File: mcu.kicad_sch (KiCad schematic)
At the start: 20 parts, among them Q8 RUM002N05T2L, Q9 RUM002N05T2L, U2 ESP32-WROOM-32D

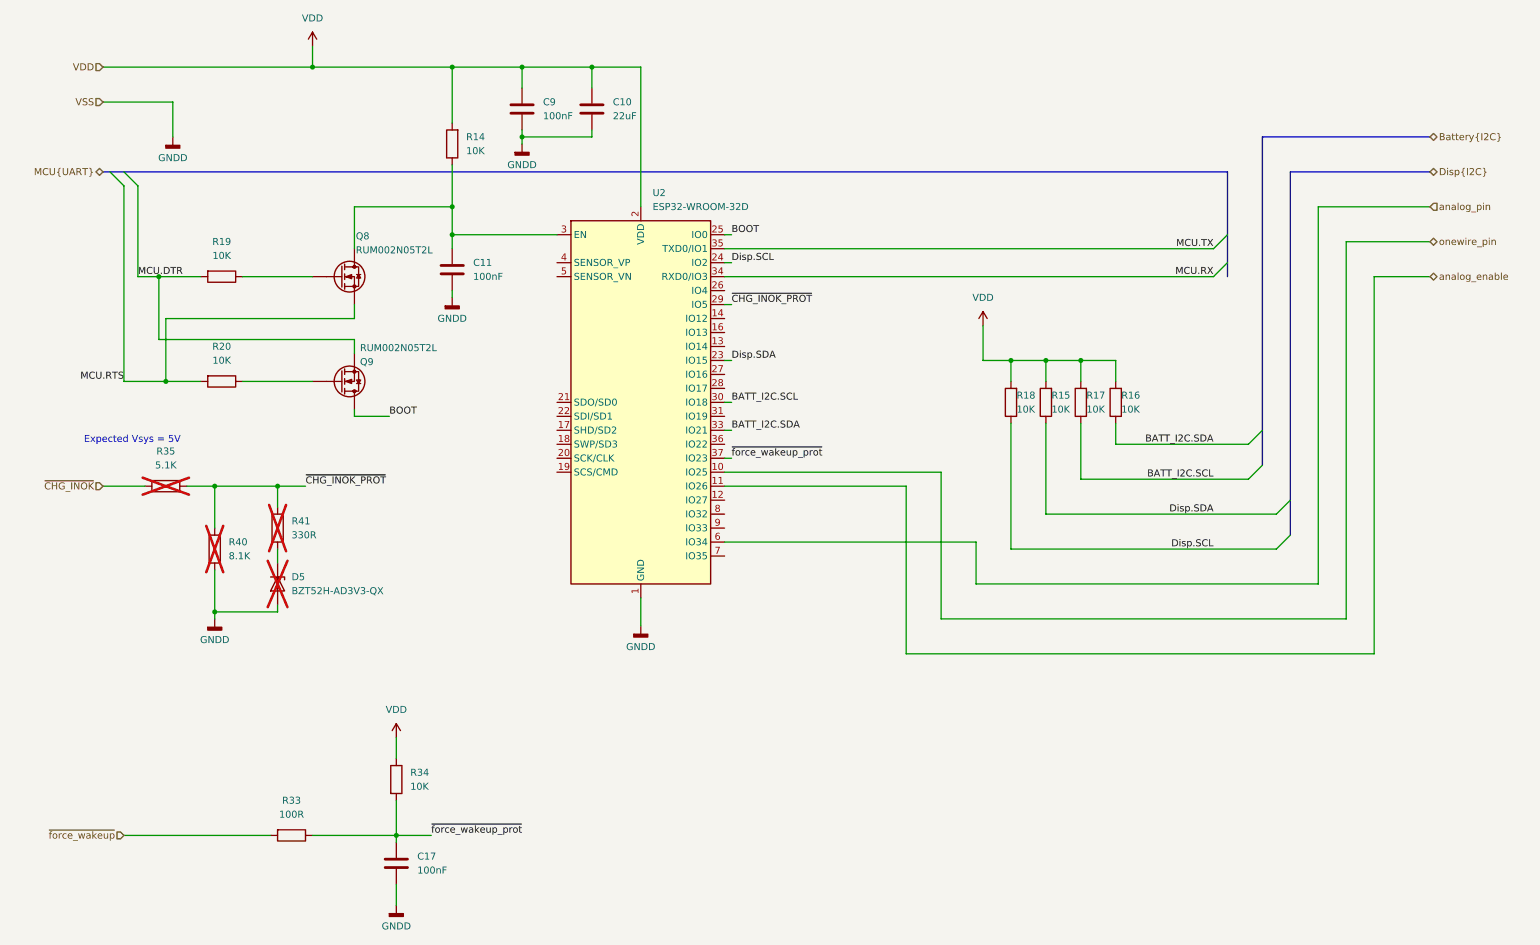
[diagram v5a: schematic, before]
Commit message: Fix issues from Issue#1
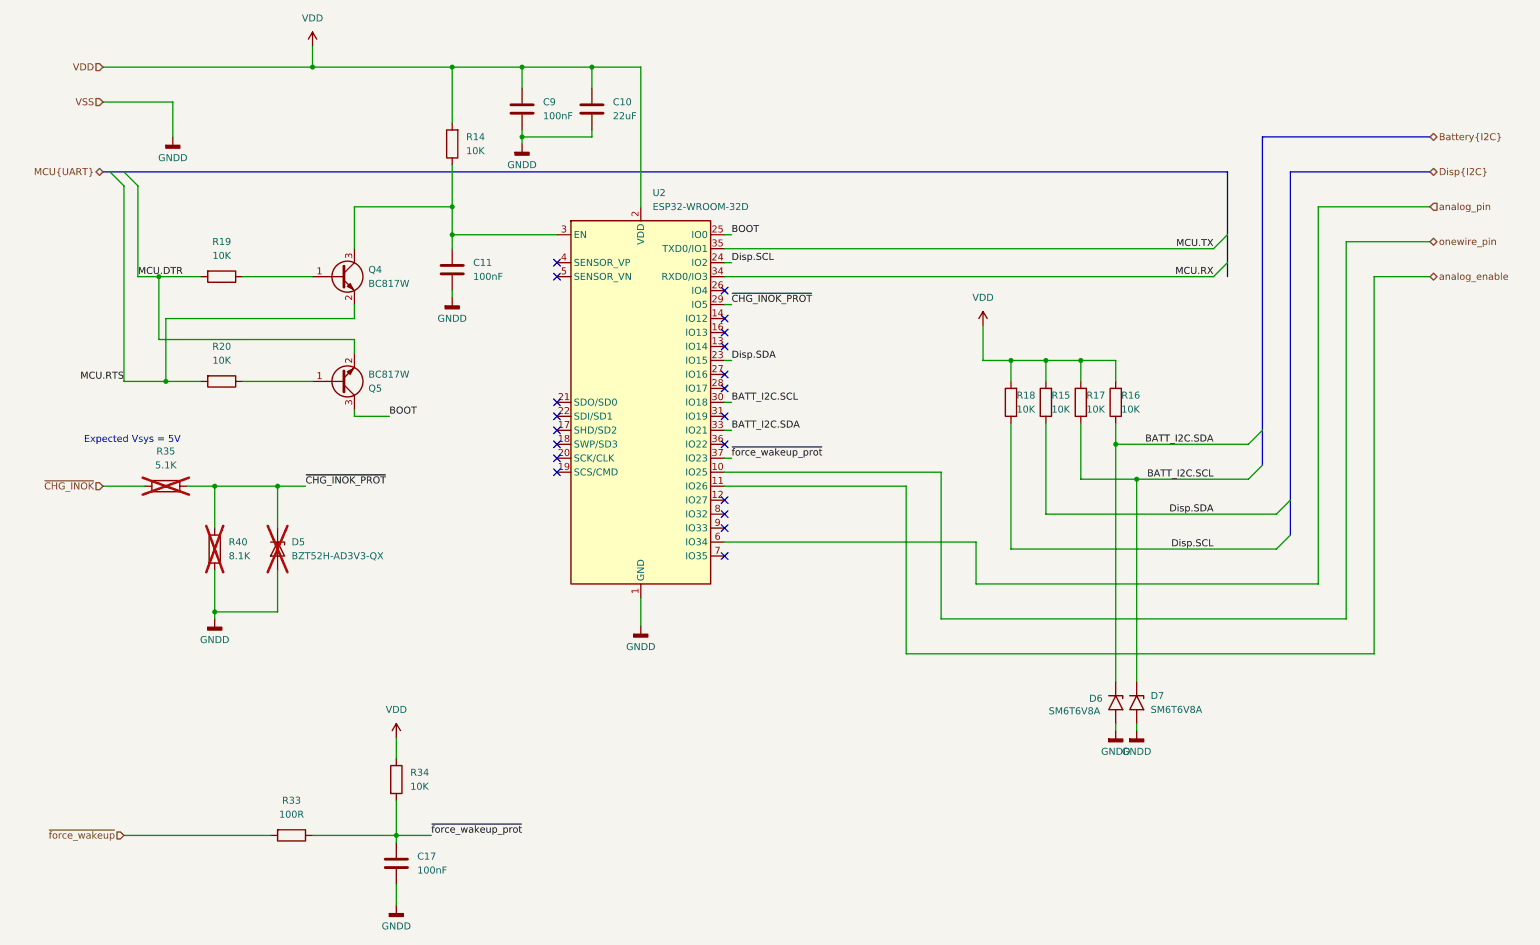
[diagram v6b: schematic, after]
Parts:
- removed Q8, Q9: RUM002N05T2L, Package_TO_SOT_SMD:SOT-723, symbol Device:Q_NMOS
- removed R41: 330R, Resistor_SMD:R_0603_1608Metric_Pad0.98x0.95mm_HandSolder, symbol Device:R
- added D6, D7: SM6T6V8A, Diode_SMD:D_SMB, symbol Diode:SM6T6V8A
- added Q4, Q5: BC817W, Package_TO_SOT_SMD:SOT-323_SC-70, symbol Transistor_BJT:BC817W
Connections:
- net BATT_I2C.SCL: now also D7.1 (A1)
- net BATT_I2C.SDA: now also D6.1 (A1)
- net BOOT: now also Q5.3 (C)
- net GNDD: now also D6.2 (A2), D7.2 (A2)
- net MCU.DTR: now also Q5.2 (E)
- net MCU.RTS: now also Q4.2 (E)
- net ~{CHG_INOK_PROT}: now also D5.1 (K)
- net at R20.1: now also Q5.1 (B)
- net at R19.1: now also Q4.1 (B)
- net at C11.1, R14.1, U2.3 (EN): now also Q4.3 (C)
- no-connect marks 0 -> 20
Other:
- moved on the sheet: D5

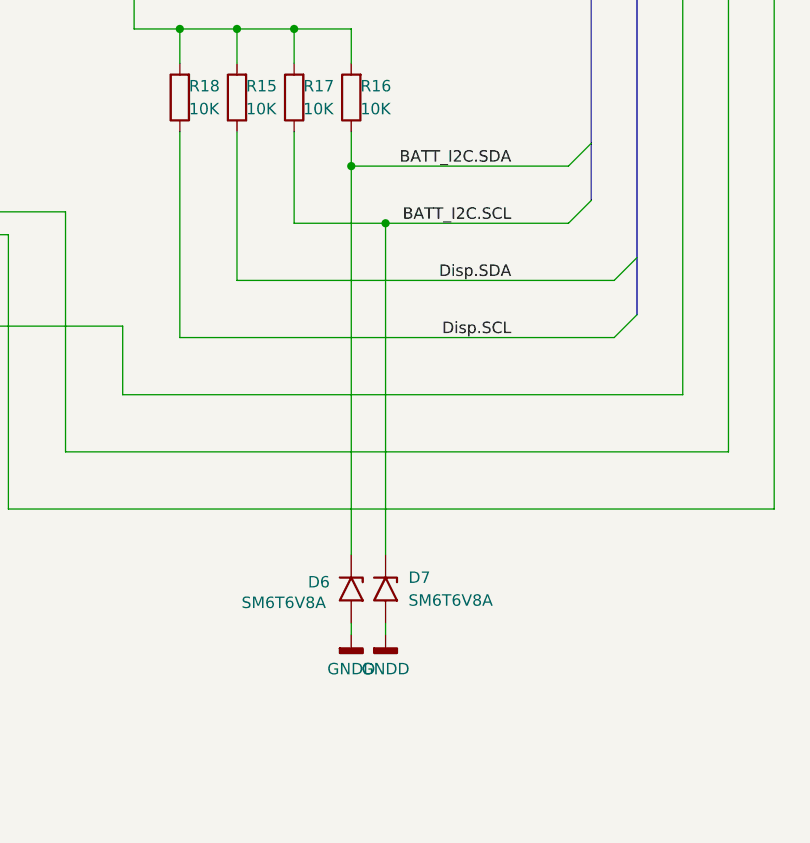
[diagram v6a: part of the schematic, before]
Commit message: Add footprint to debug connector.
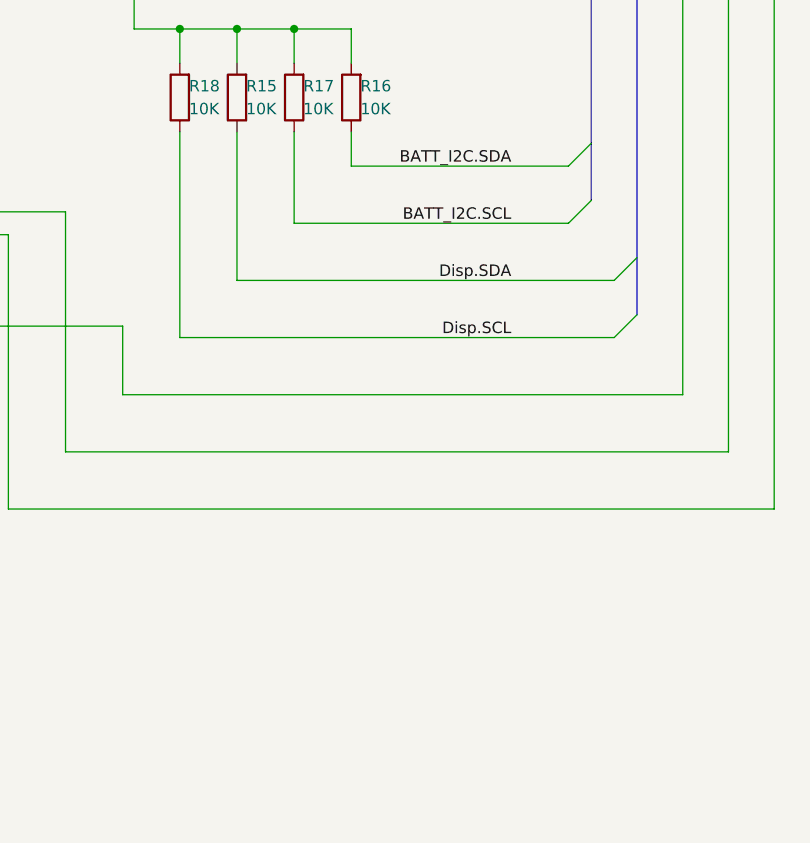
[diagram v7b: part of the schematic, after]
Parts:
- removed D6, D7: SM6T6V8A, Diode_SMD:D_SMB, symbol Diode:SM6T6V8A

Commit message: Add someplacement.
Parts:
- removed U2: ESP32-WROOM-32D, RF_Module:ESP32-WROOM-32D, symbol RF_Module:ESP32-WROOM-32D
- added U2: ESP32-WROOM-32, RF_Module:ESP32-WROOM-32, symbol RF_Module:ESP32-WROOM-32
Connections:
- net BATT_I2C.SCL: now also U2.30 (IO18)
- net BATT_I2C.SDA: now also U2.33 (IO21)
- net BOOT: now also U2.25 (IO0)
- net Disp.SCL: now also U2.24 (IO2)
- net Disp.SDA: now also U2.23 (IO15)
- net GNDD: now also U2.1 (GND), U2.15 (GND), U2.38 (GND), U2.39 (GND)
- net MCU.RX: now also U2.34 (RXD0/IO3)
- net MCU.TX: now also U2.35 (TXD0/IO1)
- net VDD: now also U2.2 (VDD)
- net analog_enable: now also U2.11 (IO26)
- net analog_pin: now also U2.6 (IO34)
- net onewire_pin: now also U2.10 (IO25)
- net ~{CHG_INOK_PROT}: now also U2.29 (IO5)
- net ~{force_wakeup_prot}: now also U2.37 (IO23)
- net at C11.1, Q4.3 (C), R14.1: now also U2.3 (EN)
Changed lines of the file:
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@@
+	)
+	(symbol
+		(lib_id "RF_Module:ESP32-WROOM-32")
+		(at 123.19 86.36 0)
+		(unit 1)
+		(body_style 1)
+		(exclude_from_sim no)
+		(in_bom yes)
+		(on_board yes)
+		(in_pos_files yes)
+		(dnp no)
+		(fields_autoplaced yes)
+		(property "Reference" "U2"
+			(at 125.3333 48.26 0)
+			(show_name no)
+			(do_not_autoplace no)
+			(effects
+				(font
+					(size 1.27 1.27)
+				)
+				(justify left)
+			)
+		)
+		(property "Value" "ESP32-WROOM-32"
+			(at 125.3333 50.8 0)
+			(show_name no)
+			(do_not_autoplace no)
+			(effects
+				(font
+					(size 1.27 1.27)
+				)
+				(justify left)
+			)
+		)
+		(property "Footprint" "RF_Module:ESP32-WROOM-32"
+			(at 123.19 124.46 0)
+			(hide yes)
+			(show_name no)
+			(do_not_autoplace no)
+			(effects
+				(font
+					(size 1.27 1.27)
+				)
+			)
+		)
+		(property "Datasheet" "https://www.espressif.com/sites/default/files/documentation/esp32-wroom-32_datasheet_en.pdf"
+			(at 115.57 85.09 0)
+			(hide yes)
+			(show_name no)
+			(do_not_autoplace no)
+			(effects
+				(font
+					(size 1.27 1.27)
+				)
+			)
+		)
+		(property "Description" "RF Module, ESP32-D0WDQ6 SoC, Wi-Fi 802.11b/g/n, Bluetooth, BLE, 32-bit, 2.7-3.6V, onboard antenna, SMD"
+			(at 123.19 86.36 0)
+			(hide yes)
+			(show_name no)
+			(do_not_autoplace no)
+			(effects
+				(font
+					(size 1.27 1.27)
+				)
+			)
+		)
+		(pin "21"
+		)
+		(pin "12"
+		)
+		(pin "36"
+		)
+		(pin "10"
+		)
+		(pin "26"
+		)
+		(pin "22"
+		)
+		(pin "31"
+		)
+		(pin "23"
+		)
+		(pin "7"
+		)
+		(pin "6"
+		)
+		(pin "5"
+		)
+		(pin "4"
+		)
+		(pin "3"
+		)
+		(pin "2"
+		)
+		(pin "1"
+		)
+		(pin "39"
+		)
+		(pin "35"
+		)
+		(pin "11"
+		)
+		(pin "19"
+		)
+		(pin "17"
+		)
+		(pin "29"
+		)
+		(pin "24"
+		)
+		(pin "8"
+		)
+		(pin "18"
+		)
+		(pin "15"
+		)
+		(pin "32"
+		)
+		(pin "27"
+		)
+		(pin "9"
+		)
+		(pin "38"
+		)
+		(pin "28"
+		)
+		(pin "13"
+		)
+		(pin "20"
+		)
+		(pin "25"
+		)
+		(pin "34"
+		)
+		(pin "30"
+		)
+		(pin "37"
+		)
+		(pin "14"
+		)
+		(pin "16"
+		)
+		(pin "33"
+		)
+		(instances
+			(project "MoistureESP"
+				(path "/f2b9f638-139e-46ec-aa60-77c4af989196/0ddaa739-ba4f-4157-bc77-184906368825"
+					(reference "U2")
+					(unit 1)
+				)
+			)
+		)
 	)
 	(symbol
@@
 					(unit 1)
 				)
-			)
-		)
-	)
-	(symbol
-		(lib_id "RF_Module:ESP32-WROOM-32D")
-		(at 123.19 86.36 0)
-		(unit 1)
-		(body_style 1)
-		(exclude_from_sim no)
-		(in_bom yes)
-		(on_board yes)
-		(in_pos_files yes)
-		(dnp no)
-		(fields_autoplaced yes)
-		(property "Reference" "U2"
-			(at 125.3333 48.26 0)
-			(show_name no)
-			(do_not_autoplace no)
-			(effects
-				(font
-					(size 1.27 1.27)
-				)
-				(justify left)
-			)
-		)
-		(property "Value" "ESP32-WROOM-32D"
-			(at 125.3333 50.8 0)
-			(show_name no)
-			(do_not_autoplace no)
-			(effects
-				(font
-					(size 1.27 1.27)
-				)
-				(justify left)
-			)
-		)
-		(property "Footprint" "RF_Module:ESP32-WROOM-32D"
-			(at 139.7 120.65 0)
-			(hide yes)
-			(show_name no)
-			(do_not_autoplace no)
-			(effects
-				(font
-					(size 1.27 1.27)
-				)
-			)
-		)
-		(property "Datasheet" "https://www.espressif.com/sites/default/files/documentation/esp32-wroom-32d_esp32-wroom-32u_datasheet_en.pdf"
-			(at 115.57 85.09 0)
-			(hide yes)
-			(show_name no)
-			(do_not_autoplace no)
-			(effects
-				(font
-					(size 1.27 1.27)
-				)
-			)
-		)
-		(property "Description" "RF Module, ESP32-D0WD SoC, Wi-Fi 802.11b/g/n, Bluetooth, BLE, 32-bit, 2.7-3.6V, onboard antenna, SMD"
-			(at 123.19 86.36 0)
-			(hide yes)
-			(show_name no)
-			(do_not_autoplace no)
-			(effects
-				(font
-					(size 1.27 1.27)
-				)
-			)
-		)
-		(pin "8"
-		)
-		(pin "10"
-		)
-		(pin "14"
-		)
-		(pin "9"
-		)
-		(pin "28"
-		)
-		(pin "24"
-		)
-		(pin "20"
-		)
-		(pin "12"
-		)
-		(pin "23"
-		)
-		(pin "38"
-		)
-		(pin "7"
-		)
-		(pin "11"
-		)
-		(pin "18"
-		)
-		(pin "36"
-		)
-		(pin "22"
-		)
-		(pin "4"
-		)
-		(pin "21"
-		)
-		(pin "34"
-		)
-		(pin "17"
-		)
-		(pin "13"
-		)
-		(pin "26"
-		)
-		(pin "19"
-		)
-		(pin "5"
-		)
-		(pin "29"
-		)
-		(pin "6"
-		)
-		(pin "25"
-		)
-		(pin "3"
-		)
-		(pin "30"
-		)
-		(pin "31"
-		)
-		(pin "33"
-		)
-		(pin "39"
-		)
-		(pin "32"
-		)
-		(pin "15"
-		)
-		(pin "37"
-		)
-		(pin "35"
-		)
-		(pin "27"
-		)
-		(pin "16"
-		)
-		(pin "2"
-		)
-		(pin "1"
-		)
-		(instances
-			(project "MoistureESP"
-				(path "/f2b9f638-139e-46ec-aa60-77c4af989196/0ddaa739-ba4f-4157-bc77-184906368825"
-					(reference "U2")
-					(unit 1)
-				)
